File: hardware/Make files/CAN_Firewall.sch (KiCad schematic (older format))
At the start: 31 parts, among them IC1 ATXMEGA128A4U-M, J1 DB9, J2 DB9, U1 MCP2551-I/SN, U2 MCP2551-I/SN, U3 MC78M05CDT, U4 TLV70033DDC, U5 PESDxL5UY

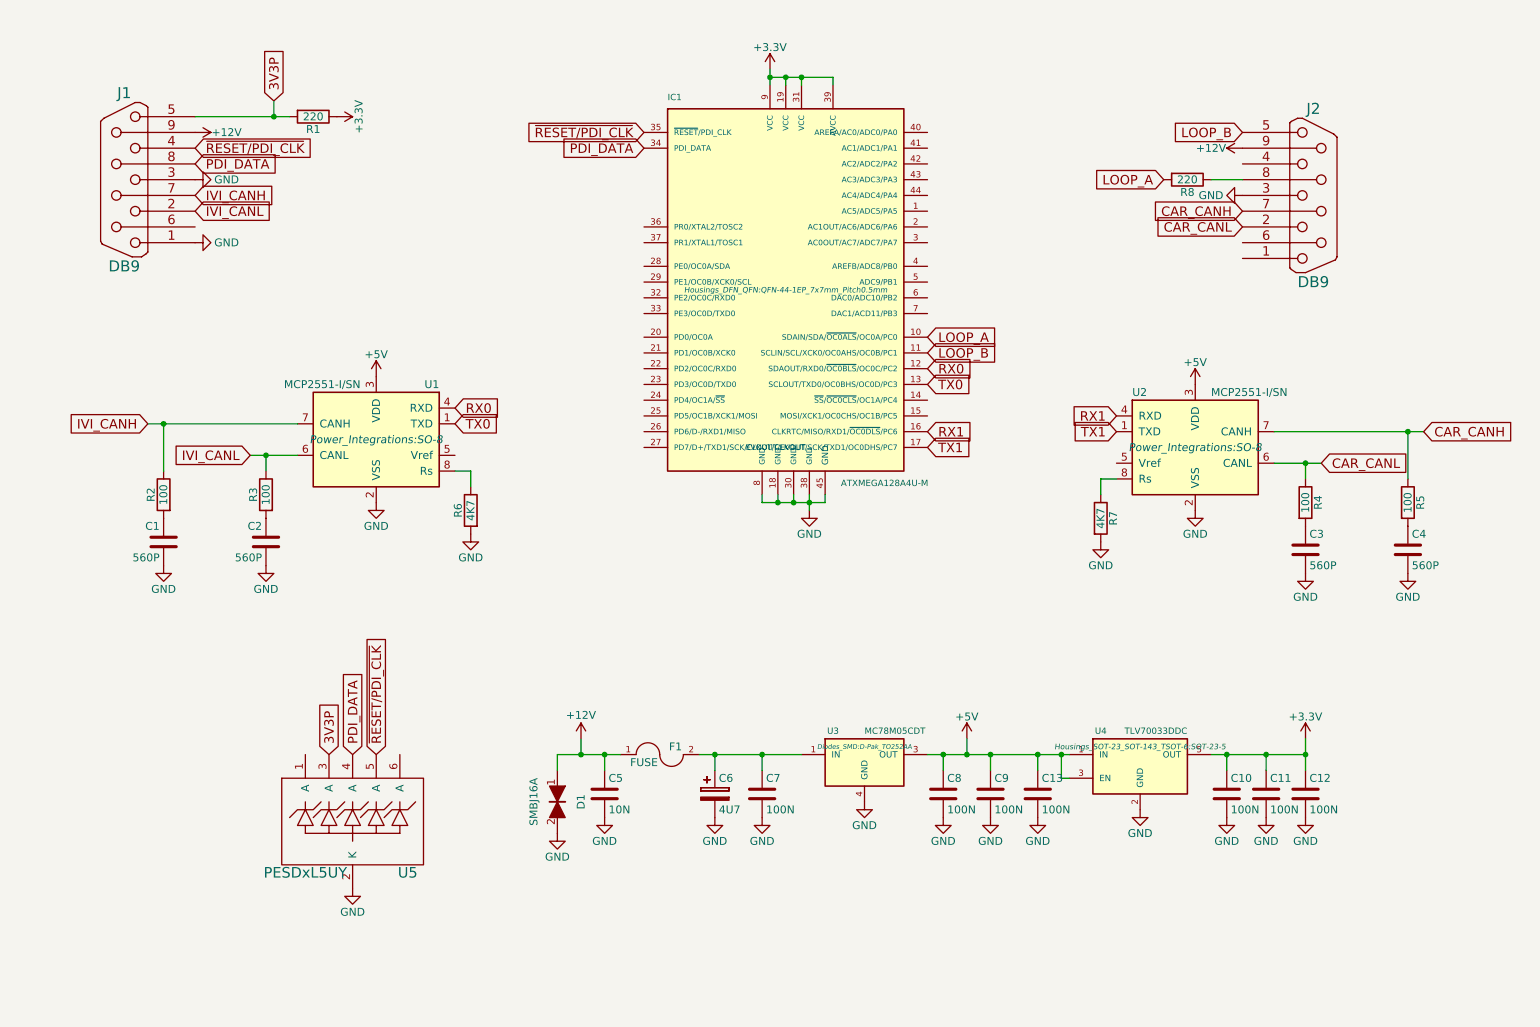
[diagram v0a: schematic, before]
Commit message: V1.1 Devlopment
Created teh V1.1 hardware files. The Hardware patch for V1 will follow
this design.
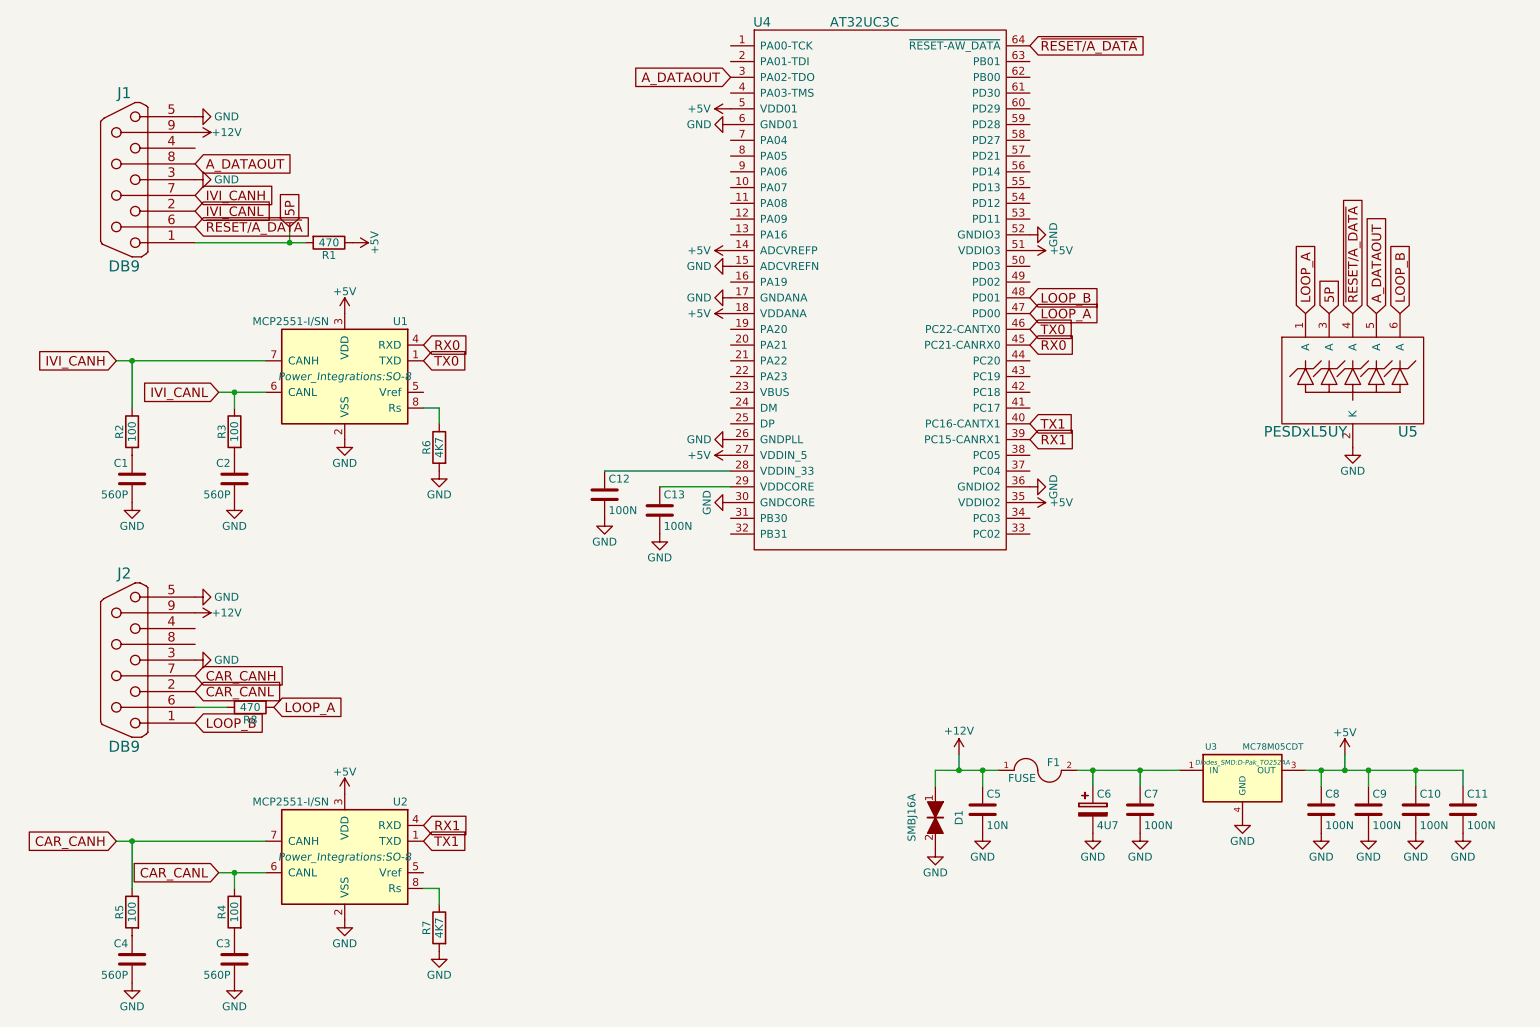
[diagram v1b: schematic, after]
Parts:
- removed IC1: ATXMEGA128A4U-M, Housings_DFN_QFN:QFN-44-1EP_7x7mm_Pitch0.5mm, symbol ATXMEGA128A4U-M-RESCUE-CAN_Firewall
- removed U4: TLV70033DDC, Housings_SOT-23_SOT-143_TSOT-6:SOT-23-5, symbol TLV70033DDC
- added U4: AT32UC3C, Housings_QFP:TQFP-64_10x10mm_Pitch0.5mm, symbol AT32UC3C
- R1, R8: value 220 -> 470
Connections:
- net +5V: now also C10.1, C11.1, R1.1, U4.14 (ADCVREFP), U4.18 (VDDANA), U4.27 (VDDIN_5), U4.35 (VDDIO2), U4.5 (VDD01), U4.51 (VDDIO3); no longer C13.1
- net GND: now also J1.5, J2.5, U4.15 (ADCVREFN), U4.17 (GNDANA), U4.26 (GNDPLL), U4.30 (GNDCORE), U4.36 (GNDIO2), U4.52 (GNDIO3), U4.6 (GND01); no longer J1.1
- net LOOP_A: now also U5.1 (A), U4.47 (PD00)
- net LOOP_B: now also J2.1, U5.6 (A), U4.48 (PD01); no longer J2.5
- net RX0: now also U4.45 (PC21-CANRX0)
- net RX1: now also U4.39 (PC15-CANRX1)
- net TX0: now also U4.46 (PC22-CANTX0)
- net TX1: now also U4.40 (PC16-CANTX1)
- net at R8.1: now also J2.6 (P6); no longer J2.8 (P8)
- net ~RESET/A_DATA: now reaches J1.6 (P6)
- net ~RESET/A_DATA: now also U5.4 (A), U4.64 (~RESET-AW_DATA)
- removed net +3V3: C10.1, C11.1, C12.1, R1.1
- net 3V3P renamed 5P
- net 5P: now also J1.1; no longer J1.5
- net PDI_DATA renamed A_DATAOUT
- net A_DATAOUT: now also U5.5 (A), U4.3 (PA02-TDO); no longer U5.4 (A)
- net ~RESET/PDI_CLK: no longer names the net of J1.4
- net ~RESET/PDI_CLK: no longer U5.5 (A)
- new net: C13.1, U4.29 (VDDCORE)
- new net: C12.1, U4.28 (VDDIN_33)
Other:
- moved on the sheet: C1, C10, C11, C12, C13, C2, C3, C4, C5, C6, C7, C8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

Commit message: V1.1 Diag port improved
added another resistor in the Loop B input, to facilitate a "bypass
mode" in conjunction with a "rule learn mode".
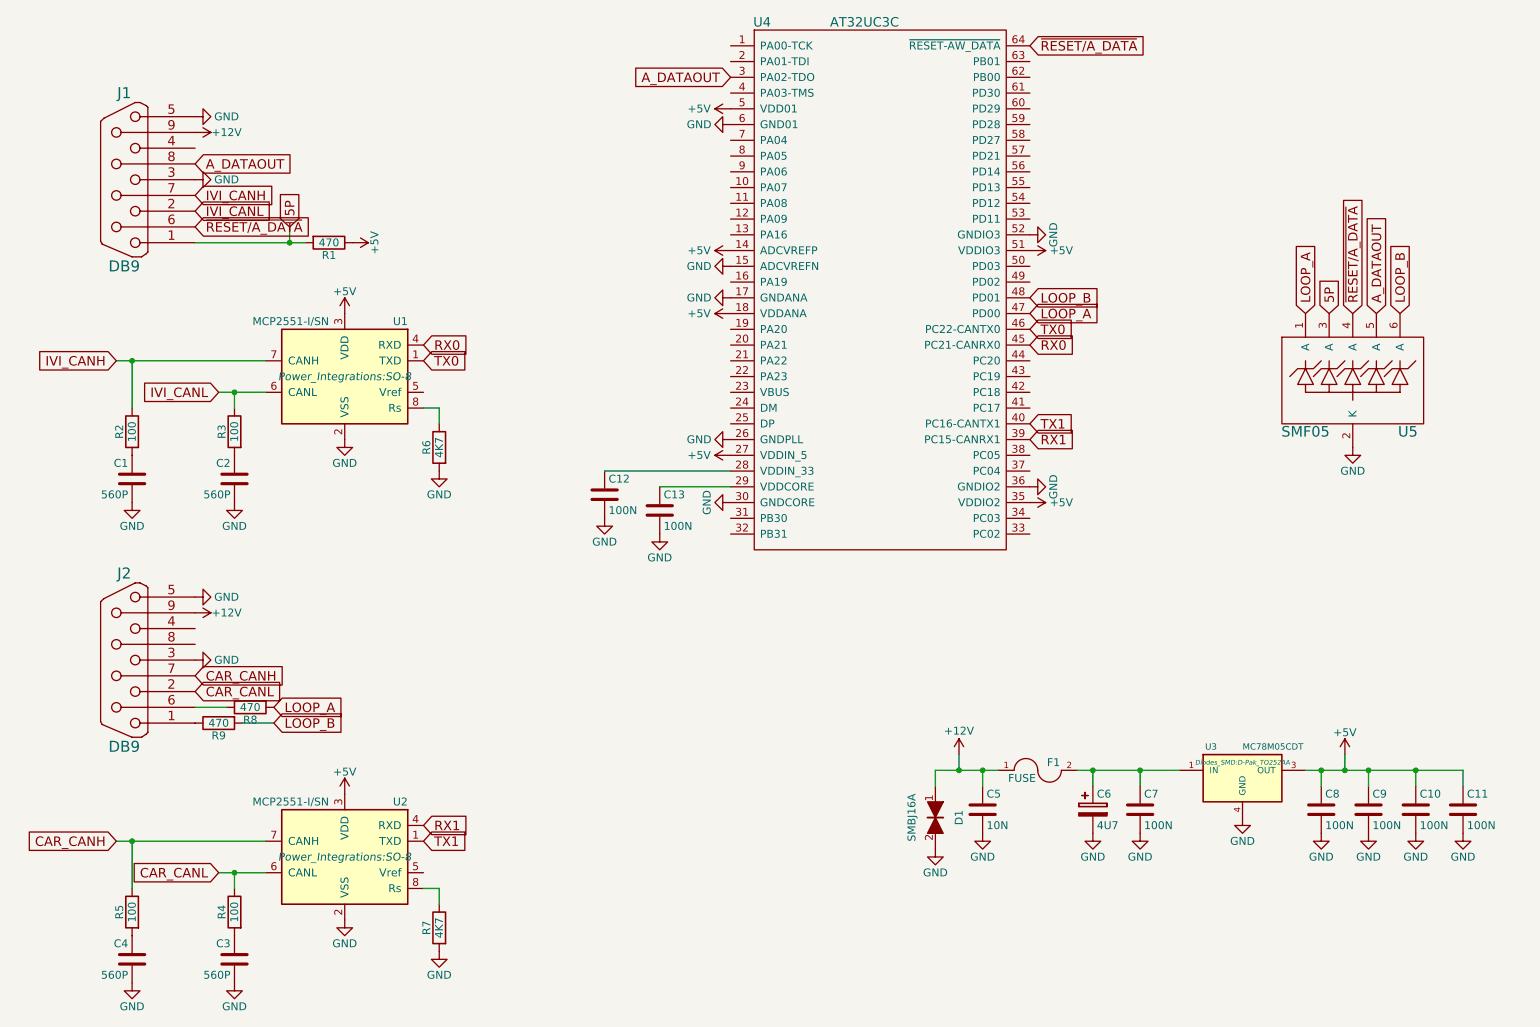
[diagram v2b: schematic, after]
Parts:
- added R9: 470, Custom Parts:R_0603_sm, symbol R
- C1, C10, C11, C12, C13, C2, C3, C4, C5, C7, C8, C9, R1, R2, R3, R4, R5, R6, R7, R8: footprint cUSTOM pARTS:R_0603_sm -> Custom Parts:R_0603_sm
- F1: footprint cUSTOM pARTS:R_1210_SM -> Custom Parts:R_1210_SM
- U5: value PESDxL5UY -> SMF05
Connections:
- net LOOP_B: now also R9.2; no longer J2.1
- new net: J2.1, R9.1
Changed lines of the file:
@@
 LIBS:contrib
 LIBS:valves
-LIBS:CUSTOM_KICAD_PART
 LIBS:CAN_Firewall-cache
 EELAYER 25 0
@@
 F 0 "C10" H 9575 6000 50  0000 L CNN
 F 1 "100N" H 9575 5800 50  0000 L CNN
-F 2 "cUSTOM pARTS:R_0603_sm" H 9588 5750 30  0001 C CNN
+F 2 "Custom Parts:R_0603_sm" H 9588 5750 30  0001 C CNN
 F 3 "" H 9550 5900 60  0000 C CNN
 	1    9550 5900
@@
 P 9150 3150
 F 0 "U5" H 9500 2800 67  0000 C CNN
-F 1 "PESDxL5UY" H 8850 2800 67  0000 C CNN
+F 1 "SMF05" H 8850 2800 67  0000 C CNN
 F 2 "Housings_SOT-23_SOT-143_TSOT-6:SC-70-6" H 9150 3200 67  0001 C CNN
 F 3 "" H 9150 3200 67  0000 C CNN
@@
 F 0 "C11" H 9875 6000 50  0000 L CNN
 F 1 "100N" H 9875 5800 50  0000 L CNN
-F 2 "cUSTOM pARTS:R_0603_sm" H 9888 5750 30  0001 C CNN
+F 2 "Custom Parts:R_0603_sm" H 9888 5750 30  0001 C CNN
 F 3 "" H 9850 5900 60  0000 C CNN
 	1    9850 5900
@@
 F 0 "C12" H 4425 4000 50  0000 L CNN
 F 1 "100N" H 4425 3800 50  0000 L CNN
-F 2 "cUSTOM pARTS:R_0603_sm" H 4438 3750 30  0001 C CNN
+F 2 "Custom Parts:R_0603_sm" H 4438 3750 30  0001 C CNN
 F 3 "" H 4400 3900 60  0000 C CNN
 	1    4400 3900
@@
 F 0 "R1" V 2730 2300 50  0000 C CNN
 F 1 "470" V 2650 2300 50  0000 C CNN
-F 2 "cUSTOM pARTS:R_0603_sm" V 2580 2300 30  0001 C CNN
+F 2 "Custom Parts:R_0603_sm" V 2580 2300 30  0001 C CNN
 F 3 "" H 2650 2300 30  0000 C CNN
 	1    2650 2300
@@
 Text GLabel 2300 5250 2    60   Input ~ 0
 LOOP_A
-Text GLabel 1800 5350 2    60   Input ~ 0
+Text GLabel 2300 5350 2    60   Input ~ 0
 LOOP_B
 $Comp
@@
 F 0 "C5" H 6825 6000 50  0000 L CNN
 F 1 "10N" H 6825 5800 50  0000 L CNN
-F 2 "cUSTOM pARTS:R_0603_sm" H 6838 5750 30  0001 C CNN
+F 2 "Custom Parts:R_0603_sm" H 6838 5750 30  0001 C CNN
 F 3 "" H 6800 5900 60  0000 C CNN
 	1    6800 5900
@@
 F 0 "C8" H 8975 6000 50  0000 L CNN
 F 1 "100N" H 8975 5800 50  0000 L CNN
-F 2 "cUSTOM pARTS:R_0603_sm" H 8988 5750 30  0001 C CNN
+F 2 "Custom Parts:R_0603_sm" H 8988 5750 30  0001 C CNN
 F 3 "" H 8950 5900 60  0000 C CNN
 	1    8950 5900
@@
 F 0 "F1" H 7250 5700 50  0000 C CNN
 F 1 "FUSE" H 7050 5600 50  0000 C CNN
-F 2 "cUSTOM pARTS:R_1210_SM" H 7150 5650 60  0001 C CNN
+F 2 "Custom Parts:R_1210_SM" H 7150 5650 60  0001 C CNN
 F 3 "" H 7150 5650 60  0000 C CNN
 	1    7150 5650
@@
 F 0 "C7" H 7825 6000 50  0000 L CNN
 F 1 "100N" H 7825 5800 50  0000 L CNN
-F 2 "cUSTOM pARTS:R_0603_sm" H 7838 5750 30  0001 C CNN
+F 2 "Custom Parts:R_0603_sm" H 7838 5750 30  0001 C CNN
 F 3 "" H 7800 5900 60  0000 C CNN
 	1    7800 5900
@@
 F 0 "C9" H 9275 6000 50  0000 L CNN
 F 1 "100N" H 9275 5800 50  0000 L CNN
-F 2 "cUSTOM pARTS:R_0603_sm" H 9288 5750 30  0001 C CNN
+F 2 "Custom Parts:R_0603_sm" H 9288 5750 30  0001 C CNN
 F 3 "" H 9250 5900 60  0000 C CNN
 	1    9250 5900
@@
 F 0 "R7" V 3430 6650 50  0000 C CNN
 F 1 "4K7" V 3350 6650 50  0000 C CNN
-F 2 "cUSTOM pARTS:R_0603_sm" V 3280 6650 30  0001 C CNN
+F 2 "Custom Parts:R_0603_sm" V 3280 6650 30  0001 C CNN
 F 3 "" H 3350 6650 30  0000 C CNN
 	1    3350 6650
@@
 F 0 "R4" V 2130 6550 50  0000 C CNN
 F 1 "100" V 2050 6550 50  0000 C CNN
-F 2 "cUSTOM pARTS:R_0603_sm" V 1980 6550 30  0001 C CNN
+F 2 "Custom Parts:R_0603_sm" V 1980 6550 30  0001 C CNN
 F 3 "" H 2050 6550 30  0000 C CNN
 	1    2050 6550
@@
 F 0 "R5" V 1480 6550 50  0000 C CNN
 F 1 "100" V 1400 6550 50  0000 C CNN
-F 2 "cUSTOM pARTS:R_0603_sm" V 1330 6550 30  0001 C CNN
+F 2 "Custom Parts:R_0603_sm" V 1330 6550 30  0001 C CNN
 F 3 "" H 1400 6550 30  0000 C CNN
 	1    1400 6550
@@
 F 0 "C3" H 2075 6950 50  0000 L CNN
 F 1 "560P" H 2075 6750 50  0000 L CNN
-F 2 "cUSTOM pARTS:R_0603_sm" H 2088 6700 30  0001 C CNN
+F 2 "Custom Parts:R_0603_sm" H 2088 6700 30  0001 C CNN
 F 3 "" H 2050 6850 60  0000 C CNN
 	1    2050 6850
@@
 F 0 "C4" H 1425 6950 50  0000 L CNN
 F 1 "560P" H 1425 6750 50  0000 L CNN
-F 2 "cUSTOM pARTS:R_0603_sm" H 1438 6700 30  0001 C CNN
+F 2 "Custom Parts:R_0603_sm" H 1438 6700 30  0001 C CNN
 F 3 "" H 1400 6850 60  0000 C CNN
 	1    1400 6850
@@
 F 0 "R6" V 3430 3600 50  0000 C CNN
 F 1 "4K7" V 3350 3600 50  0000 C CNN
-F 2 "cUSTOM pARTS:R_0603_sm" V 3280 3600 30  0001 C CNN
+F 2 "Custom Parts:R_0603_sm" V 3280 3600 30  0001 C CNN
 F 3 "" H 3350 3600 30  0000 C CNN
 	1    3350 3600
@@
 F 0 "R3" V 2130 3500 50  0000 C CNN
 F 1 "100" V 2050 3500 50  0000 C CNN
-F 2 "cUSTOM pARTS:R_0603_sm" V 1980 3500 30  0001 C CNN
+F 2 "Custom Parts:R_0603_sm" V 1980 3500 30  0001 C CNN
 F 3 "" H 2050 3500 30  0000 C CNN
 	1    2050 3500
@@
 F 0 "R2" V 1480 3500 50  0000 C CNN
 F 1 "100" V 1400 3500 50  0000 C CNN
-F 2 "cUSTOM pARTS:R_0603_sm" V 1330 3500 30  0001 C CNN
+F 2 "Custom Parts:R_0603_sm" V 1330 3500 30  0001 C CNN
 F 3 "" H 1400 3500 30  0000 C CNN
 	1    1400 3500
@@
 F 0 "C2" H 2075 3900 50  0000 L CNN
 F 1 "560P" H 2075 3700 50  0000 L CNN
-F 2 "cUSTOM pARTS:R_0603_sm" H 2088 3650 30  0001 C CNN
+F 2 "Custom Parts:R_0603_sm" H 2088 3650 30  0001 C CNN
 F 3 "" H 2050 3800 60  0000 C CNN
 	1    2050 3800
@@
 F 0 "C1" H 1425 3900 50  0000 L CNN
 F 1 "560P" H 1425 3700 50  0000 L CNN
-F 2 "cUSTOM pARTS:R_0603_sm" H 1438 3650 30  0001 C CNN
+F 2 "Custom Parts:R_0603_sm" H 1438 3650 30  0001 C CNN
 F 3 "" H 1400 3800 60  0000 C CNN
 	1    1400 3800
@@
 F 0 "R8" V 2230 5250 50  0000 C CNN
 F 1 "470" V 2150 5250 50  0000 C CNN
-F 2 "cUSTOM pARTS:R_0603_sm" V 2080 5250 30  0001 C CNN
+F 2 "Custom Parts:R_0603_sm" V 2080 5250 30  0001 C CNN
 F 3 "" H 2150 5250 30  0000 C CNN
 	1    2150 5250
@@
 F 0 "C13" H 4775 4100 50  0000 L CNN
 F 1 "100N" H 4775 3900 50  0000 L CNN
-F 2 "cUSTOM pARTS:R_0603_sm" H 4788 3850 30  0001 C CNN
+F 2 "Custom Parts:R_0603_sm" H 4788 3850 30  0001 C CNN
 F 3 "" H 4750 4000 60  0000 C CNN
 	1    4750 4000
@@
 Wire Wire Line
 	2500 2300 1800 2300
+$Comp
+L R R9
+U 1 1 55CDF193
+P 1950 5350
+F 0 "R9" V 2030 5350 50  0000 C CNN
+F 1 "470" V 1950 5350 50  0000 C CNN
+F 2 "Custom Parts:R_0603_sm" V 1880 5350 30  0001 C CNN
+F 3 "" H 1950 5350 30  0000 C CNN
+	1    1950 5350
+	0    -1   1    0
+$EndComp
+Wire Wire Line
+	2100 5350 2300 5350
 $EndSCHEMATC
